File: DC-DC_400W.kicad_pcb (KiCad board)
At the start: 2 copper layers, 120 x 70 mm, 5 parts, among them J1 Conn_01x24, J2 Conn_01x06, J3 Conn_01x10, J4 Conn_01x10

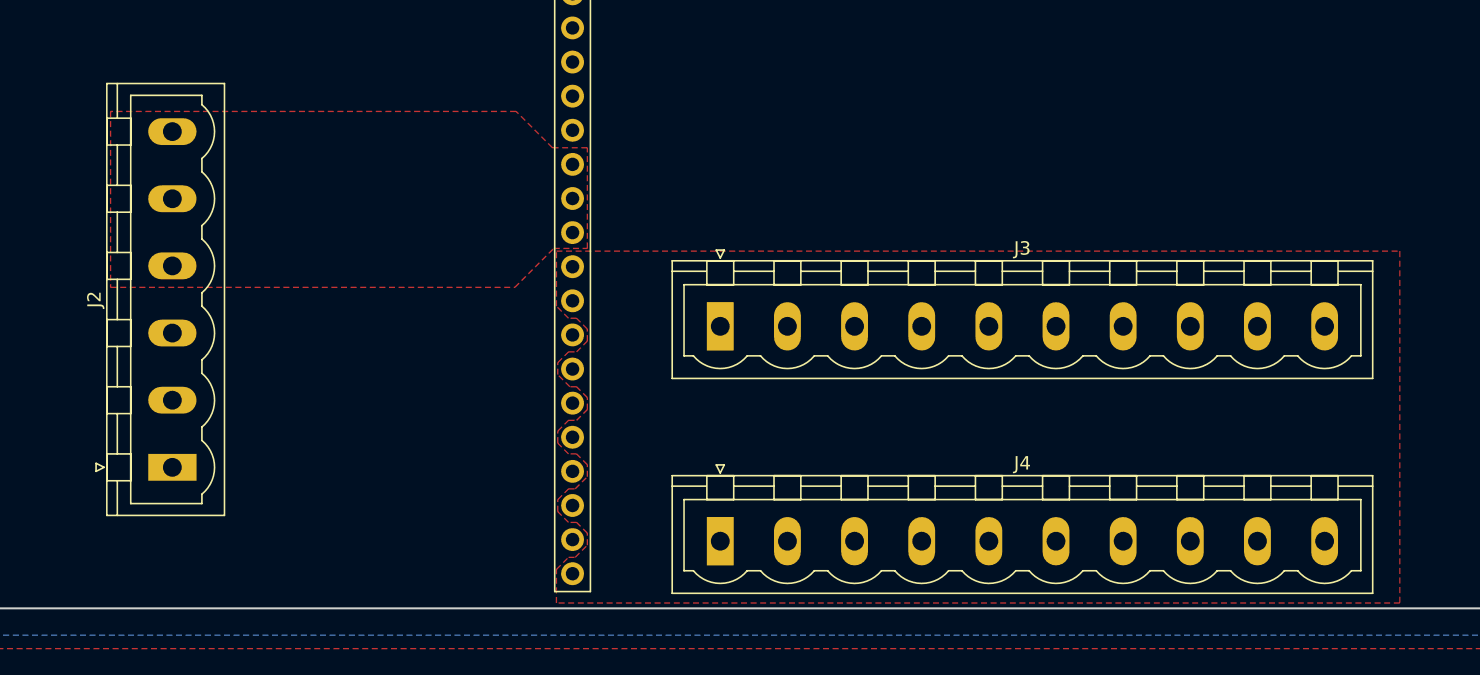
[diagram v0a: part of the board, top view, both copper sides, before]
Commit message: move to XT60 connector
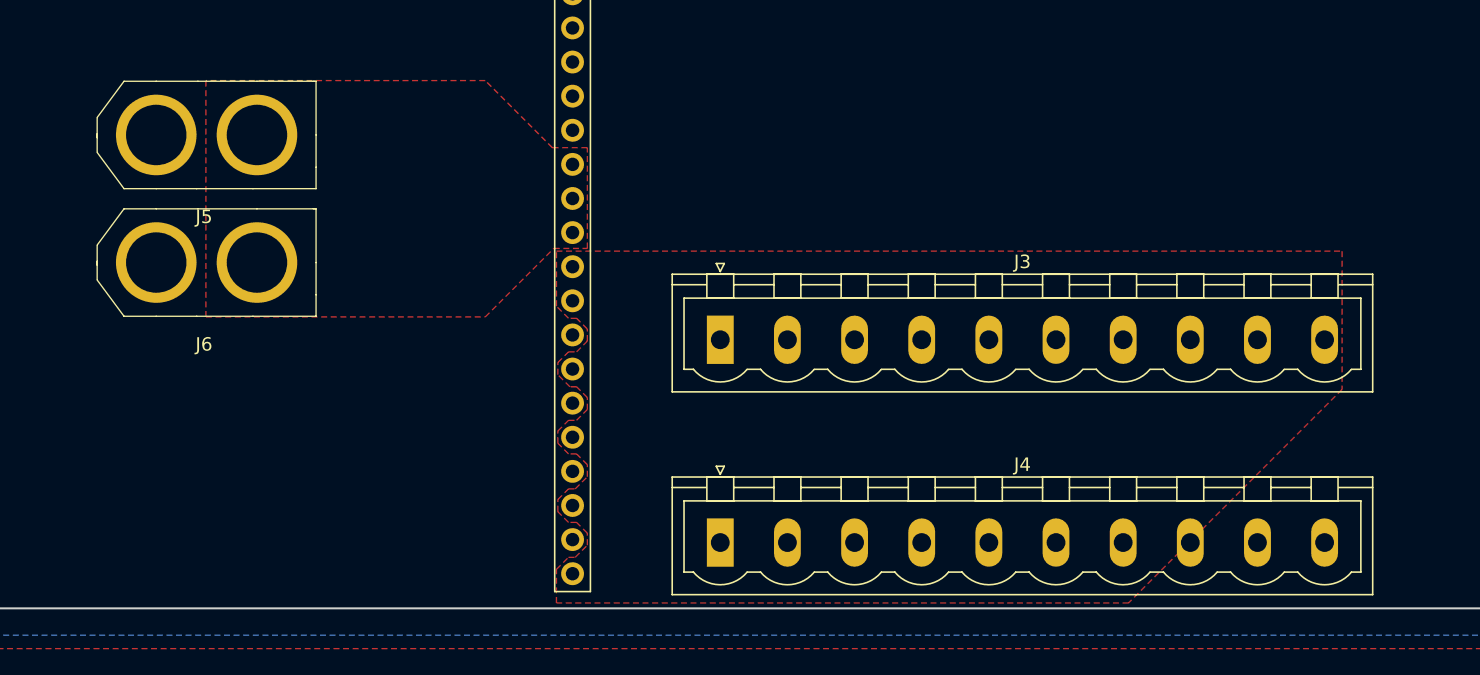
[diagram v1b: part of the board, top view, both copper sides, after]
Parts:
- removed J2: Conn_01x06, Connectors_Phoenix:PhoenixContact_MSTBVA-G_06x5.00mm_Vertical
- added J5: Conn_01x02, custom:XT60, F.Cu at (95.0, 94.8)
- added J6: Conn_01x02, custom:XT60, F.Cu at (95.0, 104.2)
- moved J3 1.00 mm to (137.0, 110.0)
- moved J4 0.10 mm to (137.0, 125.1)

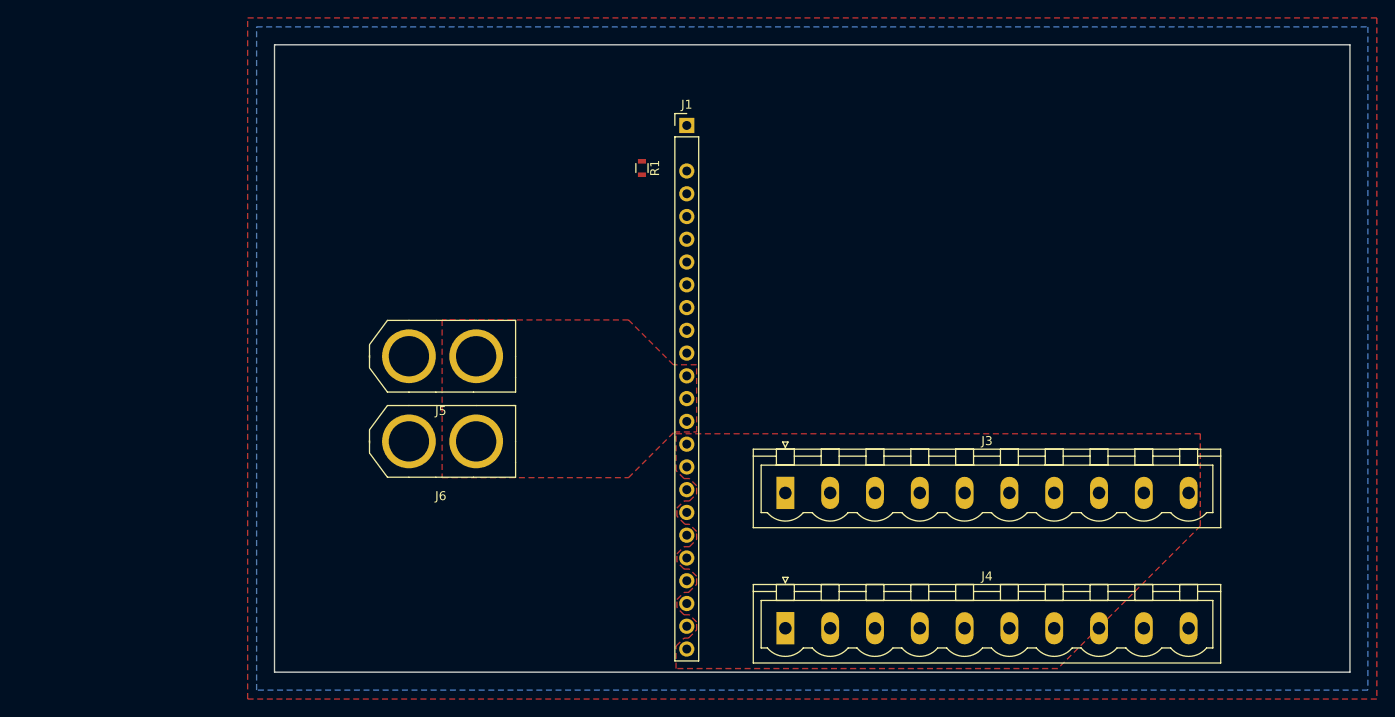
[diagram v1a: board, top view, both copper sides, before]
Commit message: only one XT60 at the input
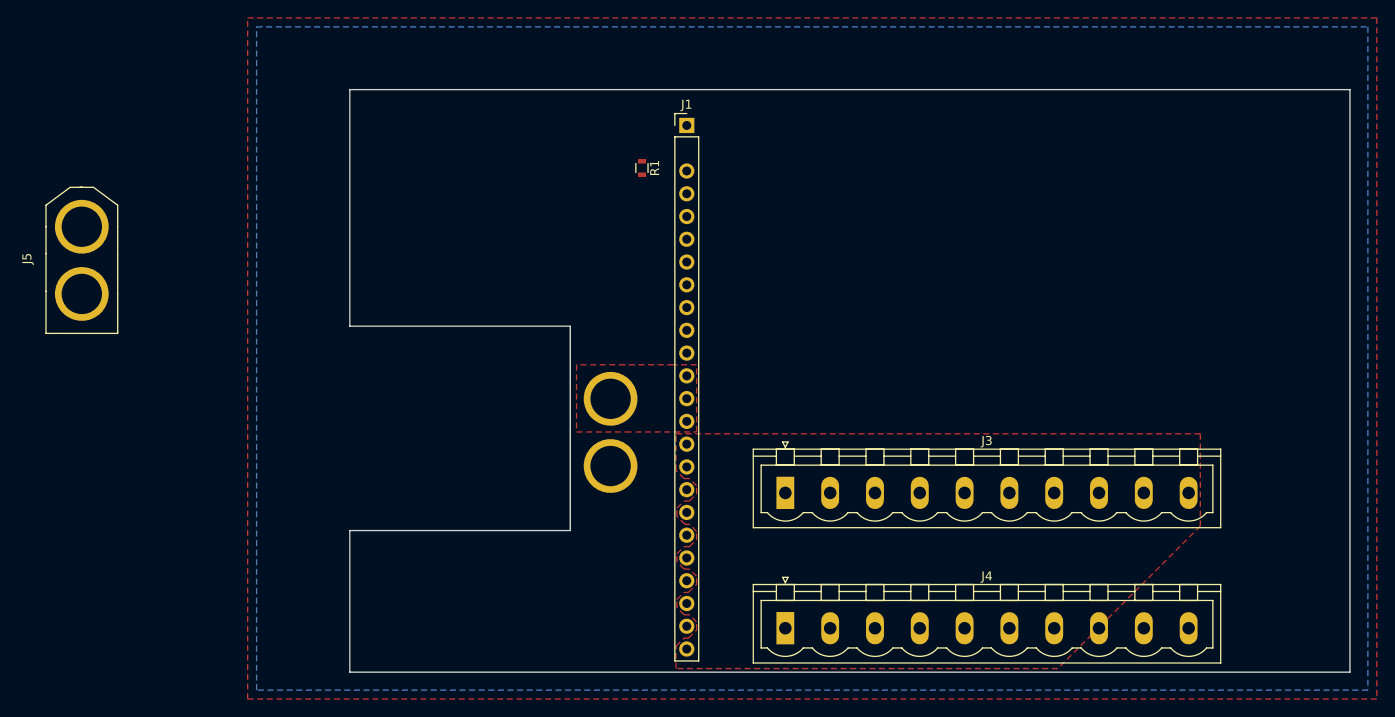
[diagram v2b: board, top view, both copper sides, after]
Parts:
- J6: moved to B.Cu
- moved J5 39.3 mm to (58.5, 80.3), turned to 270 degrees
- moved J6 22.7 mm to (117.5, 107.0), turned to 90 degrees
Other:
- board size 120 x 70 mm -> 111.6 x 65 mm
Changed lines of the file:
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@@
     (links 39)
     (no_connects 2)
-    (area 79.924999 59.924999 200.075001 130.075001)
+    (area 77 57 203.000001 133.000001)
     (thickness 1.6)
-    (drawings 7)
+    (drawings 11)
     (tracks 0)
     (zones 0)
@@
     (pad_to_mask_clearance 0.2)
     (aux_axis_origin 0 0)
-    (visible_elements FFFFFF7F)
+    (visible_elements FFFFFF3F)
     (pcbplotparams
       (layerselection 0x00030_80000001)
@@
   )
   (module custom:XT60 (layer F.Cu)
-    (at 95 94.75)
-    (fp_text reference J5 (at 3.556 6.096) (layer F.SilkS)
-      (effects (font (size 1 1) (thickness 0.15)))
-    )
-    (fp_text value Conn_01x02 (at 3.2 -5.9) (layer F.Fab)
+    (at 58.5 80.3 270)
+    (fp_text reference J5 (at 3.556 6.096 270) (layer F.SilkS)
+      (effects (font (size 1 1) (thickness 0.15)))
+    )
+    (fp_text value Conn_01x02 (at 3.2 -5.9 270) (layer F.Fab)
       (effects (font (size 1 1) (thickness 0.15)))
     )
@@
     (fp_line (start 7.5 -4) (end 3.1 -4) (layer F.SilkS) (width 0.1))
     (fp_line (start 7.2 4) (end 3 4) (layer F.SilkS) (width 0.1))
-    (pad 1 thru_hole circle (at 0 0) (size 6 6) (drill 4.5) (layers *.Cu *.Mask F.SilkS)
-      (net 2 GND))
-    (pad 2 thru_hole circle (at 7.5 0) (size 6 6) (drill 4.5) (layers *.Cu *.Mask F.SilkS)
+    (pad 1 thru_hole circle (at 0 0 270) (size 6 6) (drill 4.5) (layers *.Cu *.Mask F.SilkS)
+      (net 2 GND))
+    (pad 2 thru_hole circle (at 7.5 0 270) (size 6 6) (drill 4.5) (layers *.Cu *.Mask F.SilkS)
       (net 9 +12V))
   )
-  (module custom:XT60 (layer F.Cu)
-    (at 95 104.25)
-    (fp_text reference J6 (at 3.556 6.096) (layer F.SilkS)
-      (effects (font (size 1 1) (thickness 0.15)))
-    )
-    (fp_text value Conn_01x02 (at 3.2 -5.9) (layer F.Fab)
-      (effects (font (size 1 1) (thickness 0.15)))
-    )
-    (fp_line (start 7.2 4) (end 11.9 4) (layer F.SilkS) (width 0.1))
-    (fp_line (start 11.9 4) (end 11.9 2.4) (layer F.SilkS) (width 0.1))
-    (fp_line (start 7.5 -4) (end 11.7 -4) (layer F.SilkS) (width 0.1))
-    (fp_line (start 11.7 -4) (end 11.8 -4) (layer F.SilkS) (width 0.1))
-    (fp_line (start 11.8 -4) (end 11.9 -4) (layer F.SilkS) (width 0.1))
-    (fp_line (start 11.9 -4) (end 11.9 0) (layer F.SilkS) (width 0.1))
-    (fp_line (start -2.4 4) (end -4.4 1.3) (layer F.SilkS) (width 0.1))
-    (fp_line (start -2.4 -4) (end -4.4 -1.3) (layer F.SilkS) (width 0.1))
-    (fp_line (start -4.4 0) (end -4.4 1.25) (layer F.SilkS) (width 0.1))
-    (fp_line (start -4.4 0) (end -4.4 -1.25) (layer F.SilkS) (width 0.1))
-    (fp_line (start 0 4) (end -2.4 4) (layer F.SilkS) (width 0.1))
-    (fp_line (start 3 4) (end 0 4) (layer F.SilkS) (width 0.1))
-    (fp_line (start 0 -4) (end -2.4 -4) (layer F.SilkS) (width 0.1))
-    (fp_line (start 3.1 -4) (end 0 -4) (layer F.SilkS) (width 0.1))
-    (fp_line (start -4.4 -0.1) (end -4.4 0.2) (layer F.SilkS) (width 0.1))
-    (fp_line (start 11.9 0) (end 11.9 2.4) (layer F.SilkS) (width 0.1))
-    (fp_line (start 7.5 -4) (end 3.1 -4) (layer F.SilkS) (width 0.1))
-    (fp_line (start 7.2 4) (end 3 4) (layer F.SilkS) (width 0.1))
-    (pad 1 thru_hole circle (at 0 0) (size 6 6) (drill 4.5) (layers *.Cu *.Mask F.SilkS)
-      (net 2 GND))
-    (pad 2 thru_hole circle (at 7.5 0) (size 6 6) (drill 4.5) (layers *.Cu *.Mask F.SilkS)
+  (module custom:XT60 (layer B.Cu)
+    (at 117.5 107 90)
+    (fp_text reference J6 (at 3.556 -6.096 90) (layer B.SilkS)
+      (effects (font (size 1 1) (thickness 0.15)) (justify mirror))
+    )
+    (fp_text value Conn_01x02 (at 3.2 5.9 90) (layer B.Fab)
+      (effects (font (size 1 1) (thickness 0.15)) (justify mirror))
+    )
+    (fp_line (start 7.2 -4) (end 11.9 -4) (layer B.SilkS) (width 0.1))
+    (fp_line (start 11.9 -4) (end 11.9 -2.4) (layer B.SilkS) (width 0.1))
+    (fp_line (start 7.5 4) (end 11.7 4) (layer B.SilkS) (width 0.1))
+    (fp_line (start 11.7 4) (end 11.8 4) (layer B.SilkS) (width 0.1))
+    (fp_line (start 11.8 4) (end 11.9 4) (layer B.SilkS) (width 0.1))
+    (fp_line (start 11.9 4) (end 11.9 0) (layer B.SilkS) (width 0.1))
+    (fp_line (start -2.4 -4) (end -4.4 -1.3) (layer B.SilkS) (width 0.1))
+    (fp_line (start -2.4 4) (end -4.4 1.3) (layer B.SilkS) (width 0.1))
+    (fp_line (start -4.4 0) (end -4.4 -1.25) (layer B.SilkS) (width 0.1))
+    (fp_line (start -4.4 0) (end -4.4 1.25) (layer B.SilkS) (width 0.1))
+    (fp_line (start 0 -4) (end -2.4 -4) (layer B.SilkS) (width 0.1))
+    (fp_line (start 3 -4) (end 0 -4) (layer B.SilkS) (width 0.1))
+    (fp_line (start 0 4) (end -2.4 4) (layer B.SilkS) (width 0.1))
+    (fp_line (start 3.1 4) (end 0 4) (layer B.SilkS) (width 0.1))
+    (fp_line (start -4.4 0.1) (end -4.4 -0.2) (layer B.SilkS) (width 0.1))
+    (fp_line (start 11.9 0) (end 11.9 -2.4) (layer B.SilkS) (width 0.1))
+    (fp_line (start 7.5 4) (end 3.1 4) (layer B.SilkS) (width 0.1))
+    (fp_line (start 7.2 -4) (end 3 -4) (layer B.SilkS) (width 0.1))
+    (pad 1 thru_hole circle (at 0 0 90) (size 6 6) (drill 4.5) (layers *.Cu *.Mask B.SilkS)
+      (net 2 GND))
+    (pad 2 thru_hole circle (at 7.5 0 90) (size 6 6) (drill 4.5) (layers *.Cu *.Mask B.SilkS)
       (net 9 +12V))
   )
+  (gr_line (start 88.4 91.4) (end 88.4 65) (layer Edge.Cuts) (width 0.15))
+  (gr_line (start 113 91.4) (end 88.4 91.4) (layer Edge.Cuts) (width 0.15))
+  (gr_line (start 113 114.2) (end 88.4 114.2) (layer Edge.Cuts) (width 0.15))
+  (gr_line (start 88.4 114.2) (end 88.4 130) (layer Edge.Cuts) (width 0.15))
   (dimension 20 (width 0.3) (layer Eco1.User)
     (gr_text "20,000 mm" (at 104 96.450001) (layer Eco1.User)
@@
     (arrow2b (pts (xy 126 97.700001) (xy 124.873496 98.286422)))
   )
-  (gr_line (start 126 99.5) (end 85.3 99.5) (layer Eco2.User) (width 0.05))
-  (gr_line (start 80 60) (end 80 130) (layer Edge.Cuts) (width 0.15))
-  (gr_line (start 200 60) (end 80 60) (layer Edge.Cuts) (width 0.15))
-  (gr_line (start 200 130) (end 200 60) (layer Edge.Cuts) (width 0.15))
-  (gr_line (start 80 130) (end 200 130) (layer Edge.Cuts) (width 0.15))
+  (gr_line (start 126 99.5) (end 112.4 99.5) (layer Eco2.User) (width 0.05))
+  (gr_line (start 113 91.4) (end 113 114.2) (layer Edge.Cuts) (width 0.15))
+  (gr_line (start 200 65) (end 88.4 65) (layer Edge.Cuts) (width 0.15))
+  (gr_line (start 200 130) (end 200 65) (layer Edge.Cuts) (width 0.15))
+  (gr_line (start 88.4 130) (end 200 130) (layer Edge.Cuts) (width 0.15))
   (zone (net 9) (net_name +12V) (layer F.Cu) (hatch edge 0.508)
     (priority 2)
@@
     (polygon
       (pts
-        (xy 127.1 95.7) (xy 124.5 95.7) (xy 119.5 90.7) (xy 98.7 90.7) (xy 98.7 108.3)
-        (xy 119.5 108.3) (xy 124.6 103.2) (xy 127.1 103.2)
+        (xy 127.1 95.7) (xy 124.5 95.7) (xy 119.1 95.7) (xy 113.7 95.7) (xy 113.7 103.2)
+        (xy 119.2 103.2) (xy 124.6 103.2) (xy 127.1 103.2)
       )
     )

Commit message: remove unused XT60 connector, shrink pcb
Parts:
- removed J5: Conn_01x02, custom:XT60
- moved R1 1.35 mm to (122.2, 74.2)
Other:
- board size 111.6 x 65 mm -> 98.2 x 63 mm
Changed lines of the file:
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@@
 (kicad_pcb (version 4) (host pcbnew 4.0.7-e2-6376~58~ubuntu16.04.1)
   (general
-    (links 39)
+    (links 37)
     (no_connects 2)
-    (area 77 57 203.000001 133.000001)
+    (area 88.324999 64.924999 200.075001 130.075001)
     (thickness 1.6)
     (drawings 11)
     (tracks 0)
     (zones 0)
-    (modules 6)
+    (modules 5)
     (nets 11)
   )
@@
   )
   (module Resistors_SMD:R_0603 (layer F.Cu)
-    (at 121 73.75 270)
+    (at 122.25 74.25 270)
     (descr "Resistor SMD 0603, reflow soldering, Vishay (see dcrcw.pdf)")
     (tags "resistor 0603")
@@
     )
   )
-  (module custom:XT60 (layer F.Cu)
-    (at 58.5 80.3 270)
-    (fp_text reference J5 (at 3.556 6.096 270) (layer F.SilkS)
-      (effects (font (size 1 1) (thickness 0.15)))
-    )
-    (fp_text value Conn_01x02 (at 3.2 -5.9 270) (layer F.Fab)
-      (effects (font (size 1 1) (thickness 0.15)))
-    )
-    (fp_line (start 7.2 4) (end 11.9 4) (layer F.SilkS) (width 0.1))
-    (fp_line (start 11.9 4) (end 11.9 2.4) (layer F.SilkS) (width 0.1))
-    (fp_line (start 7.5 -4) (end 11.7 -4) (layer F.SilkS) (width 0.1))
-    (fp_line (start 11.7 -4) (end 11.8 -4) (layer F.SilkS) (width 0.1))
-    (fp_line (start 11.8 -4) (end 11.9 -4) (layer F.SilkS) (width 0.1))
-    (fp_line (start 11.9 -4) (end 11.9 0) (layer F.SilkS) (width 0.1))
-    (fp_line (start -2.4 4) (end -4.4 1.3) (layer F.SilkS) (width 0.1))
-    (fp_line (start -2.4 -4) (end -4.4 -1.3) (layer F.SilkS) (width 0.1))
-    (fp_line (start -4.4 0) (end -4.4 1.25) (layer F.SilkS) (width 0.1))
-    (fp_line (start -4.4 0) (end -4.4 -1.25) (layer F.SilkS) (width 0.1))
-    (fp_line (start 0 4) (end -2.4 4) (layer F.SilkS) (width 0.1))
-    (fp_line (start 3 4) (end 0 4) (layer F.SilkS) (width 0.1))
-    (fp_line (start 0 -4) (end -2.4 -4) (layer F.SilkS) (width 0.1))
-    (fp_line (start 3.1 -4) (end 0 -4) (layer F.SilkS) (width 0.1))
-    (fp_line (start -4.4 -0.1) (end -4.4 0.2) (layer F.SilkS) (width 0.1))
-    (fp_line (start 11.9 0) (end 11.9 2.4) (layer F.SilkS) (width 0.1))
-    (fp_line (start 7.5 -4) (end 3.1 -4) (layer F.SilkS) (width 0.1))
-    (fp_line (start 7.2 4) (end 3 4) (layer F.SilkS) (width 0.1))
-    (pad 1 thru_hole circle (at 0 0 270) (size 6 6) (drill 4.5) (layers *.Cu *.Mask F.SilkS)
-      (net 2 GND))
-    (pad 2 thru_hole circle (at 7.5 0 270) (size 6 6) (drill 4.5) (layers *.Cu *.Mask F.SilkS)
-      (net 9 +12V))
-  )
   (module custom:XT60 (layer B.Cu)
     (at 117.5 107 90)
@@
       (net 9 +12V))
   )
-  (gr_line (start 88.4 91.4) (end 88.4 65) (layer Edge.Cuts) (width 0.15))
-  (gr_line (start 113 91.4) (end 88.4 91.4) (layer Edge.Cuts) (width 0.15))
-  (gr_line (start 113 114.2) (end 88.4 114.2) (layer Edge.Cuts) (width 0.15))
-  (gr_line (start 88.4 114.2) (end 88.4 130) (layer Edge.Cuts) (width 0.15))
-  (dimension 20 (width 0.3) (layer Eco1.User)
-    (gr_text "20,000 mm" (at 104 96.450001) (layer Eco1.User)
+  (dimension 15 (width 0.3) (layer Eco1.User)
+    (gr_text "15,000 mm" (at 106.5 88.15) (layer Eco1.User)
       (effects (font (size 1.5 1.5) (thickness 0.3)))
     )
-    (feature1 (pts (xy 94 99.5) (xy 94 95.100001)))
-    (feature2 (pts (xy 114 99.5) (xy 114 95.100001)))
-    (crossbar (pts (xy 114 97.800001) (xy 94 97.800001)))
-    (arrow1a (pts (xy 94 97.800001) (xy 95.126504 97.21358)))
-    (arrow1b (pts (xy 94 97.800001) (xy 95.126504 98.386422)))
-    (arrow2a (pts (xy 114 97.800001) (xy 112.873496 97.21358)))
-    (arrow2b (pts (xy 114 97.800001) (xy 112.873496 98.386422)))
-  )
+    (feature1 (pts (xy 99 97) (xy 99 86.8)))
+    (feature2 (pts (xy 114 97) (xy 114 86.8)))
+    (crossbar (pts (xy 114 89.5) (xy 99 89.5)))
+    (arrow1a (pts (xy 99 89.5) (xy 100.126504 88.913579)))
+    (arrow1b (pts (xy 99 89.5) (xy 100.126504 90.086421)))
+    (arrow2a (pts (xy 114 89.5) (xy 112.873496 88.913579)))
+    (arrow2b (pts (xy 114 89.5) (xy 112.873496 90.086421)))
+  )
+  (gr_line (start 88.5 91.5) (end 88.5 66.75) (layer Edge.Cuts) (width 0.15))
+  (gr_line (start 113 91.5) (end 88.5 91.5) (layer Edge.Cuts) (width 0.15))
+  (gr_line (start 113 114) (end 88.5 114) (layer Edge.Cuts) (width 0.15))
+  (gr_line (start 88.5 114) (end 88.5 129.75) (layer Edge.Cuts) (width 0.15))
   (dimension 12 (width 0.3) (layer Eco1.User)
     (gr_text "12,000 mm" (at 120 96.350001) (layer Eco1.User)
@@
   )
   (gr_line (start 126 99.5) (end 112.4 99.5) (layer Eco2.User) (width 0.05))
-  (gr_line (start 113 91.4) (end 113 114.2) (layer Edge.Cuts) (width 0.15))
-  (gr_line (start 200 65) (end 88.4 65) (layer Edge.Cuts) (width 0.15))
-  (gr_line (start 200 130) (end 200 65) (layer Edge.Cuts) (width 0.15))
-  (gr_line (start 88.4 130) (end 200 130) (layer Edge.Cuts) (width 0.15))
+  (gr_line (start 113 91.5) (end 113 114) (layer Edge.Cuts) (width 0.15))
+  (gr_line (start 186.75 66.75) (end 88.5 66.75) (layer Edge.Cuts) (width 0.15))
+  (gr_line (start 186.75 129.75) (end 186.75 66.75) (layer Edge.Cuts) (width 0.15))
+  (gr_line (start 88.5 129.75) (end 186.75 129.75) (layer Edge.Cuts) (width 0.15))
   (zone (net 9) (net_name +12V) (layer F.Cu) (hatch edge 0.508)
     (priority 2)

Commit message: some progress on pcb
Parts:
- added J2: Conn_01x03, Connectors:Fan_Pin_Header_Straight_1x03, F.Cu at (141.2, 88.0)
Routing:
- net GND: track 0.00 -> 250.3 mm, vias 0 -> 3
- net +5V: track 0.00 -> 57.2 mm
- net +12V: track 0.00 -> 28.5 mm
- net /TRIM+: track 0.00 -> 6.70 mm
- net /TRIM-: track 0.00 -> 5.71 mm
- added copper zone on B.Cu, net +12V
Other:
- board size 98.2 x 63 mm -> 96 x 63 mm
- net class Default: clearance 0.2 -> 0.25
- rule trace_clearance: 0.2 -> 0.25
